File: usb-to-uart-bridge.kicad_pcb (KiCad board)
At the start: 2 copper layers, 32 x 16 mm, 10 parts, among them J1 USB_C_Receptacle_USB2.0_16P, J2 Conn_01x05_Pin, U1 CP2102N-Axx-xQFN28

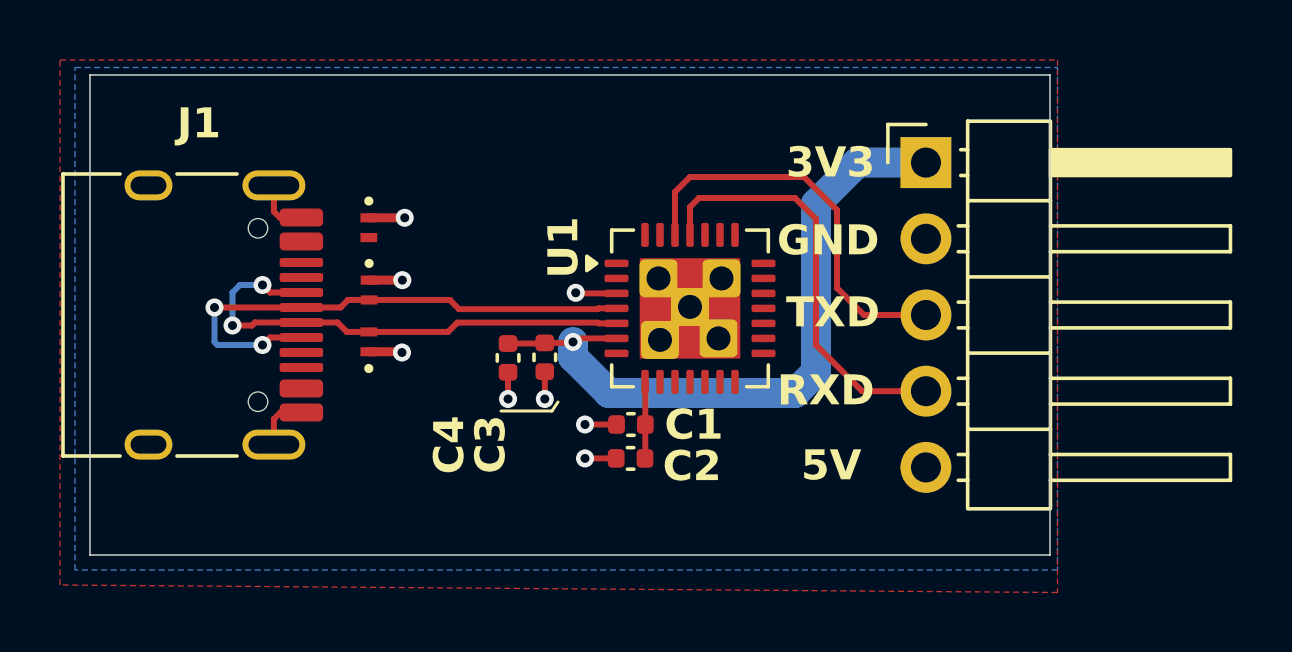
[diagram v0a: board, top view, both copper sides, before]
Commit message: Updated Schematic and Layout with CC Resistors
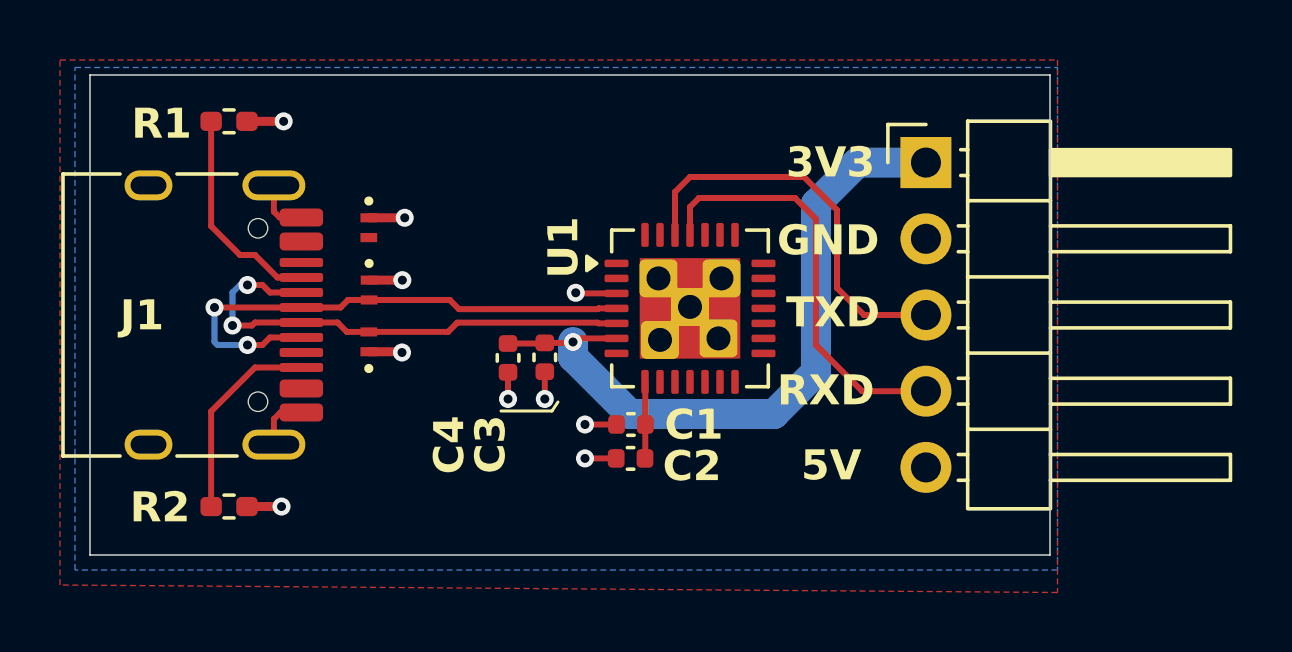
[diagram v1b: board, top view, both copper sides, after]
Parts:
- added R1: 5.1K, Resistor_SMD:R_0402_1005Metric_Pad0.72x0.64mm_HandSolder, F.Cu at (124.6, 81.5)
- added R2: 5.1K, Resistor_SMD:R_0402_1005Metric_Pad0.72x0.64mm_HandSolder, F.Cu at (124.6, 94.4)
- U1: value CP2102N-Axx-xQFN28 -> CP2102N
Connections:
- J1 pad A5: unconnected-(J1-CC1-PadA5) -> Net-(J1-CC1)
- J1 pad B5: unconnected-(J1-CC2-PadB5) -> Net-(J1-CC2)
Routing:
- net Net-(J1-CC1): track 0.00 -> 7.21 mm
- net Net-(J1-CC2): track 0.00 -> 6.79 mm
- net GND: track 12.5 -> 14.8 mm, vias 8 -> 10
- net VDD: track 22.9 -> 23.5 mm
